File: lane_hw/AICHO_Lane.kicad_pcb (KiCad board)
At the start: 2 copper layers, 0 parts

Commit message: lane_hw: DC-DC
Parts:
- added C11: 10u 50V, Capacitor_SMD:C_0805_2012Metric, F.Cu at (86.3, 50.2)
- added C12: 10u 50V, Capacitor_SMD:C_0805_2012Metric, F.Cu at (84.3, 50.2)
- added C13: 100n, Capacitor_SMD:C_0402_1005Metric, F.Cu at (82.8, 50.8)
- added C14: 100n, Capacitor_SMD:C_0402_1005Metric, F.Cu at (78.5, 49.2)
- added C15: 22u 25V, Capacitor_SMD:C_0805_2012Metric, F.Cu at (77.2, 51.1)
- added C16: 22u 25V, Capacitor_SMD:C_0805_2012Metric, F.Cu at (77.2, 53.1)
- added C17: 33p, Capacitor_SMD:C_0402_1005Metric, F.Cu at (81.3, 47.2)
- added L1: 15u, Inductor_SMD:L_Sunlord_SWPA5040S, F.Cu at (81.8, 55.0)
- added R11: 200k, Resistor_SMD:R_0402_1005Metric, F.Cu at (80.4, 47.2)
- added R12: 27k, Resistor_SMD:R_0402_1005Metric, F.Cu at (79.0, 47.6)
- added U1: TPS54302, Package_TO_SOT_SMD:SOT-23-6, F.Cu at (80.7, 50.2)
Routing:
- net +5V: track 0.00 -> 14.5 mm
- net Net-(U1-SW): track 0.00 -> 10.6 mm, vias 0 -> 2
- net +24V: track 0.00 -> 4.80 mm
- net GND: track 0.00 -> 3.83 mm, vias 0 -> 21
- net Net-(U1-FB): track 0.00 -> 3.32 mm
- net Net-(U1-BOOT): track 0.00 -> 1.37 mm

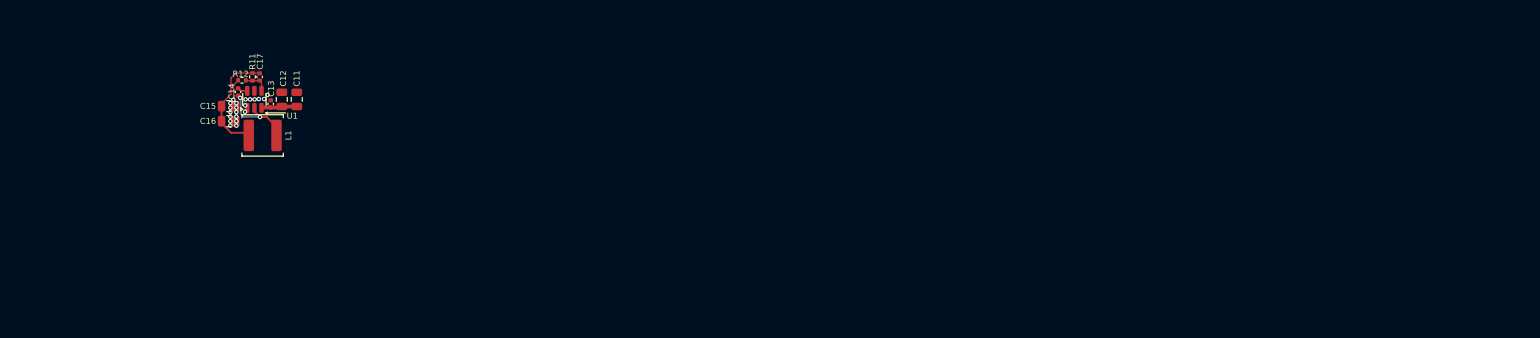
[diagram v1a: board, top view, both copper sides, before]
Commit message: lane_hw: Preliminary layout
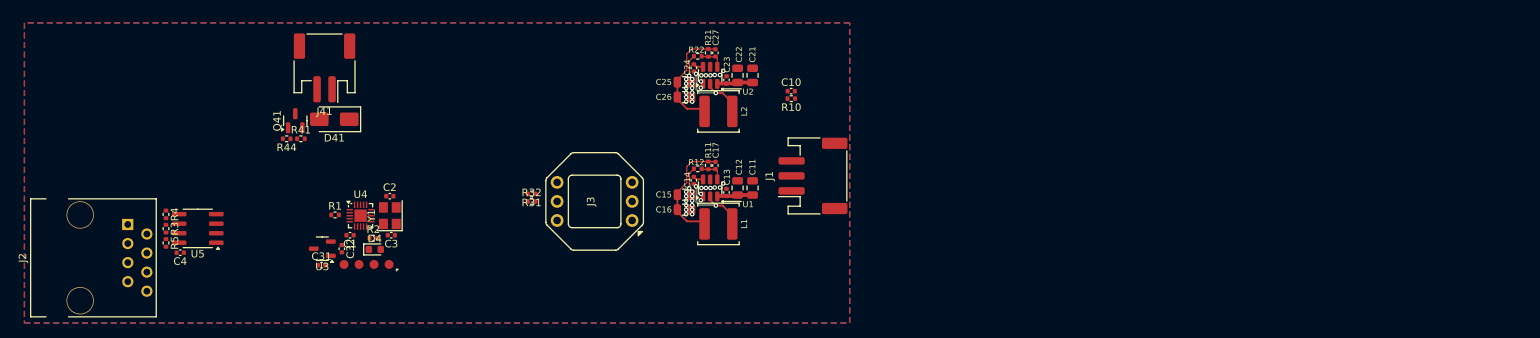
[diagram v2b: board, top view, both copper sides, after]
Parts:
- added C1: 100n, Capacitor_SMD:C_0402_1005Metric, F.Cu at (93.4, 68.3)
- added C10: 100n, Capacitor_SMD:C_0402_1005Metric, F.Cu at (152.2, 49.1)
- added C2: 15p, Capacitor_SMD:C_0402_1005Metric, F.Cu at (98.7, 63.1)
- added C21: 10u 50V, Capacitor_SMD:C_0805_2012Metric, F.Cu at (147.1, 47.0)
- added C22: 10u 50V, Capacitor_SMD:C_0805_2012Metric, F.Cu at (145.1, 47.0)
- added C23: 100n, Capacitor_SMD:C_0402_1005Metric, F.Cu at (143.6, 47.6)
- added C24: 100n, Capacitor_SMD:C_0402_1005Metric, F.Cu at (139.2, 46.0)
- added C25: 22u 25V, Capacitor_SMD:C_0805_2012Metric, F.Cu at (138.0, 47.9)
- added C26: 22u 25V, Capacitor_SMD:C_0805_2012Metric, F.Cu at (138.0, 49.9)
- added C27: 100p, Capacitor_SMD:C_0402_1005Metric, F.Cu at (142.1, 44.0)
- added C3: 15p, Capacitor_SMD:C_0402_1005Metric, F.Cu at (98.9, 68.3)
- added C31: 1u, Capacitor_SMD:C_0402_1005Metric, F.Cu at (89.6, 72.3)
- added C32: 1u, Capacitor_SMD:C_0402_1005Metric, F.Cu at (92.3, 70.1)
- added C4: 100n, Capacitor_SMD:C_0402_1005Metric, F.Cu at (70.8, 70.6)
- added D4: White, LED_SMD:LED_0603_1608Metric, F.Cu at (96.7, 70.2)
- added D41: SS14, Diode_SMD:D_SMA, F.Cu at (91.3, 52.9)
- added J1: JST PH, Connector_JST:JST_PH_S3B-PH-SM4-TB_1x03-1MP_P2.00mm_Horizontal, F.Cu at (155.1, 60.4)
- added J2: RJ45, RJ45:RJ45_OST_PJ012-8P8CX_Vertical, F.Cu at (63.8, 66.9)
- added J3: XGZP6847A, XGZP6847A:XGZP6847A, F.Cu at (126.0, 63.8)
- added J41: JST PH, Connector_JST:JST_PH_S2B-PH-SM4-TB_1x02-1MP_P2.00mm_Horizontal, F.Cu at (90.0, 46.0)
- added J9: Conn_01x04, TestPoints_P2.00:TestPoints_1x04_P2.00, F.Cu at (95.6, 72.2)
- added L2: 15u, Inductor_SMD:L_Sunlord_SWPA5040S, F.Cu at (142.5, 51.8)
- added Q41: AO3400A, Package_TO_SOT_SMD:SOT-23, F.Cu at (86.1, 53.0)
- added R1: 1k, Resistor_SMD:R_0402_1005Metric, F.Cu at (91.4, 65.6)
- added R10: 4.7, Resistor_SMD:R_0402_1005Metric, F.Cu at (152.2, 50.1)
- added R2: 5.1k, Resistor_SMD:R_0402_1005Metric, F.Cu at (96.5, 68.7)
- added R21: 100k, Resistor_SMD:R_0402_1005Metric, F.Cu at (141.2, 44.0)
- added R22: 5.1k, Resistor_SMD:R_0402_1005Metric, F.Cu at (139.8, 44.5)
- added R3: 100, Resistor_SMD:R_0402_1005Metric, F.Cu at (68.9, 67.4)
- added R31: 20k, Resistor_SMD:R_0402_1005Metric, F.Cu at (117.6, 62.8)
- added R32: 51k, Resistor_SMD:R_0402_1005Metric, F.Cu at (117.6, 63.8)
- added R4: 10k, Resistor_SMD:R_0402_1005Metric, F.Cu at (68.9, 65.5)
- added R41: 100k, Resistor_SMD:R_0402_1005Metric, F.Cu at (86.8, 55.5)
- added R44: 100, Resistor_SMD:R_0402_1005Metric, F.Cu at (85.0, 55.5)
- added R5: 10k, Resistor_SMD:R_0402_1005Metric, F.Cu at (68.9, 69.3)
- added U2: TPS54302, Package_TO_SOT_SMD:SOT-23-6, F.Cu at (141.4, 47.0)
- added U3: XC6206P332MR, Package_TO_SOT_SMD:SOT-23-3, F.Cu at (89.7, 70.1)
- added U4: PY32F003F18U6, Package_DFN_QFN:QFN-20-1EP_3x3mm_P0.4mm_EP1.65x1.65mm, F.Cu at (94.8, 65.7)
- added U5: SP485E, Package_SO:SOIC-8_3.9x4.9mm_P1.27mm, F.Cu at (73.1, 67.4)
- added Y1: 16MHz 9pF, Crystal:Crystal_SMD_3225-4Pin_3.2x2.5mm, F.Cu at (98.7, 65.7)
- moved C11 61.9 mm to (147.1, 62.0)
- moved C12 61.9 mm to (145.1, 62.0)
- moved C14 61.9 mm to (139.2, 61.0)
- moved C15 61.9 mm to (138.0, 62.9)
- moved C16 61.9 mm to (138.0, 64.9)
- moved C17 61.9 mm to (142.1, 59.0)
- moved L1 61.9 mm to (142.5, 66.8)
- moved R11 61.9 mm to (141.2, 59.0)
- moved R12 61.9 mm to (139.8, 59.5)
- moved U1 61.9 mm to (141.4, 62.0)
- moved C13 61.9 mm to (143.6, 62.6)
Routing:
- net +12V: track 0.00 -> 14.5 mm
- net Net-(U2-SW): track 0.00 -> 10.6 mm, vias 0 -> 2
- net +24V: track 4.80 -> 9.60 mm
- net GND: track 3.83 -> 7.66 mm, vias 21 -> 42
- net Net-(U2-FB): track 0.00 -> 3.32 mm
- net Net-(U2-BOOT): track 0.00 -> 1.37 mm
- added copper zone on B.Cu, net GND
- added copper zone on F.Cu, net GND

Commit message: lane_hw: Attempting to adjust layout
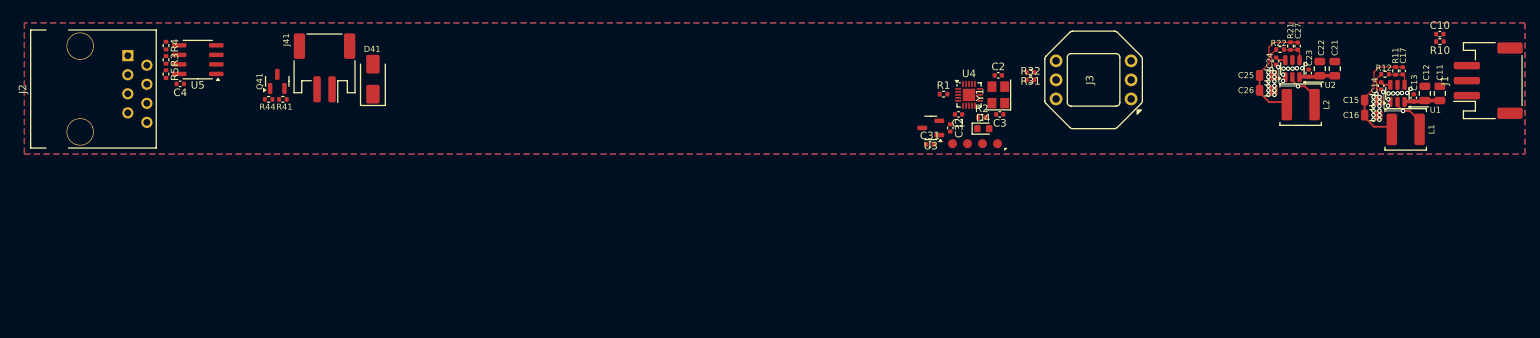
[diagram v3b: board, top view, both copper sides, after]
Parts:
- moved C13 92.5 mm to (235.2, 50.0)
- moved C11 92.5 mm to (238.7, 49.4)
- moved C12 92.5 mm to (236.7, 49.4)
- moved C14 92.5 mm to (230.8, 48.4)
- moved C15 92.5 mm to (229.6, 50.3)
- moved C16 92.5 mm to (229.6, 52.3)
- moved C17 92.5 mm to (233.7, 46.4)
- moved L1 92.5 mm to (234.1, 54.2)
- moved R11 92.5 mm to (232.8, 46.4)
- moved R12 92.5 mm to (231.3, 46.9)
- moved U1 92.5 mm to (233.0, 49.4)
- moved J1 90.9 mm to (245.1, 47.7)
- moved C10 86.8 mm to (238.7, 41.5)
- moved R10 86.8 mm to (238.7, 42.5)
- moved C2 82.7 mm to (179.8, 47.0)
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
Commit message: lane_hw: Reassign pins
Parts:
- moved D4 7.13 mm to (184.9, 53.5), turned to 180 degrees
- moved R1 5.44 mm to (176.9, 52.7), turned to 90 degrees
- moved R2 4.92 mm to (182.4, 53.7)
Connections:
- U4 pad 1: /PUMP_2 -> /UART2_RX
- U4 pad 10: unconnected-(U4-PB6-Pad10) -> /UART1_TX
- U4 pad 16: /UART2_TX -> /PRESSURE_SENSOR
- U4 pad 17: /UART2_RX -> /PUMP_3
- U4 pad 18: /DE -> /PUMP_2
- U4 pad 19: /PRESSURE_SENSOR -> /PUMP_1
- U4 pad 2: /PUMP_3 -> /DE
- U4 pad 20: /PUMP_1 -> /UART2_TX
- U4 pad 3: /UART1_TX -> unconnected-(U4-PA7-Pad3)
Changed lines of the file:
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@@
 	(net 37 "unconnected-(U4-PF2-Pad15)")
 	(net 38 "unconnected-(U4-PB5-Pad9)")
-	(net 39 "unconnected-(U4-PB6-Pad10)")
-	(net 40 "unconnected-(U4-PF4-Pad12)")
+	(net 39 "unconnected-(U4-PF4-Pad12)")
+	(net 40 "unconnected-(U4-PA7-Pad3)")
 	(footprint "Capacitor_SMD:C_0805_2012Metric"
 		(layer "F.Cu")
@@
 	(footprint "Resistor_SMD:R_0402_1005Metric"
 		(layer "F.Cu")
-		(at 172.5 49.5)
+		(at 176.9 52.7 90)
 		(descr "Resistor SMD 0402 (1005 Metric), square (rectangular) end terminal, IPC-7351 nominal, (Body size source: IPC-SM-782 page 72, https://www.pcb-3d.com/wordpress/wp-content/uploads/ipc-sm-782a_amendment_1_and_2.pdf), generated with kicad-footprint-generator")
 		(tags "resistor")
 		(property "Reference" "R1"
-			(at 0 -1.17 0)
+			(at 0 -1.17 90)
 			(layer "F.SilkS")
 			(effects
@@
 		)
 		(property "Value" "1k"
-			(at 0 1.17 0)
+			(at 0 1.17 90)
 			(layer "F.Fab")
 			(effects
@@
 		)
 		(property "Datasheet" ""
-			(at 0 0 0)
+			(at 0 0 90)
 			(layer "F.Fab")
 			(hide yes)
@@
 		)
 		(property "Description" "Resistor"
-			(at 0 0 0)
+			(at 0 0 90)
 			(layer "F.Fab")
 			(hide yes)
@@
 		)
 		(fp_line
-			(start -0.93 -0.47)
-			(end 0.93 -0.47)
+			(start 0.93 -0.47)
+			(end 0.93 0.47)
 			(stroke
 				(width 0.05)
@@
 		)
 		(fp_line
-			(start -0.93 0.47)
-			(end -0.93 -0.47)
+			(start -0.93 -0.47)
+			(end 0.93 -0.47)
 			(stroke
 				(width 0.05)
@@
 		)
 		(fp_line
-			(start 0.93 -0.47)
-			(end 0.93 0.47)
+			(start 0.93 0.47)
+			(end -0.93 0.47)
 			(stroke
 				(width 0.05)
@@
 		)
 		(fp_line
-			(start 0.93 0.47)
-			(end -0.93 0.47)
+			(start -0.93 0.47)
+			(end -0.93 -0.47)
 			(stroke
 				(width 0.05)
@@
 		)
 		(fp_line
-			(start -0.525 -0.27)
-			(end 0.525 -0.27)
+			(start 0.525 -0.27)
+			(end 0.525 0.27)
 			(stroke
 				(width 0.1)
@@
 		)
 		(fp_line
-			(start -0.525 0.27)
-			(end -0.525 -0.27)
+			(start -0.525 -0.27)
+			(end 0.525 -0.27)
 			(stroke
 				(width 0.1)
@@
 		)
 		(fp_line
-			(start 0.525 -0.27)
-			(end 0.525 0.27)
+			(start 0.525 0.27)
+			(end -0.525 0.27)
 			(stroke
 				(width 0.1)
@@
 		)
 		(fp_line
-			(start 0.525 0.27)
-			(end -0.525 0.27)
+			(start -0.525 0.27)
+			(end -0.525 -0.27)
 			(stroke
 				(width 0.1)
@@
 		)
 		(fp_text user "${REFERENCE}"
-			(at 0 0 0)
+			(at 0 0 90)
 			(layer "F.Fab")
 			(effects
@@
 		)
 		(pad "1" smd roundrect
-			(at -0.51 0)
+			(at -0.51 0 90)
 			(size 0.54 0.64)
 			(layers "F.Cu" "F.Mask" "F.Paste")
@@
 		)
 		(pad "2" smd roundrect
-			(at 0.51 0)
+			(at 0.51 0 90)
 			(size 0.54 0.64)
 			(layers "F.Cu" "F.Mask" "F.Paste")
@@
 			(layers "F.Cu" "F.Mask" "F.Paste")
 			(roundrect_rratio 0.25)
-			(net 30 "/PUMP_2")
+			(net 35 "/UART2_RX")
 			(pinfunction "PA5")
 			(pintype "bidirectional")
@@
 			(layers "F.Cu" "F.Mask" "F.Paste")
 			(roundrect_rratio 0.25)
-			(net 31 "/PUMP_3")
+			(net 33 "/DE")
 			(pinfunction "PA6")
 			(pintype "bidirectional")
@@
 			(layers "F.Cu" "F.Mask" "F.Paste")
 			(roundrect_rratio 0.25)
-			(net 26 "/UART1_TX")
+			(net 40 "unconnected-(U4-PA7-Pad3)")
 			(pinfunction "PA7")
-			(pintype "bidirectional")
+			(pintype "bidirectional+no_connect")
 		)
 		(pad "4" smd roundrect
@@
 			(layers "F.Cu" "F.Mask" "F.Paste")
 			(roundrect_rratio 0.25)
-			(net 39 "unconnected-(U4-PB6-Pad10)")
+			(net 26 "/UART1_TX")
 			(pinfunction "PB6")
-			(pintype "bidirectional+no_connect")
+			(pintype "bidirectional")
 		)
 		(pad "11" smd roundrect
@@
 			(layers "F.Cu" "F.Mask" "F.Paste")
 			(roundrect_rratio 0.25)
-			(net 40 "unconnected-(U4-PF4-Pad12)")
+			(net 39 "unconnected-(U4-PF4-Pad12)")
 			(pinfunction "PF4")
 			(pintype "bidirectional+no_connect")
@@
 			(layers "F.Cu" "F.Mask" "F.Paste")
 			(roundrect_rratio 0.25)
-			(net 34 "/UART2_TX")
+			(net 28 "/PRESSURE_SENSOR")
 			(pinfunction "PA0")
 			(pintype "bidirectional")
@@
 			(layers "F.Cu" "F.Mask" "F.Paste")
 			(roundrect_rratio 0.25)
-			(net 35 "/UART2_RX")
+			(net 31 "/PUMP_3")
 			(pinfunction "PA1")
 			(pintype "bidirectional")
@@
 			(layers "F.Cu" "F.Mask" "F.Paste")
 			(roundrect_rratio 0.25)
-			(net 33 "/DE")
+			(net 30 "/PUMP_2")
 			(pinfunction "PA2")
 			(pintype "bidirectional")
@@
 			(layers "F.Cu" "F.Mask" "F.Paste")
 			(roundrect_rratio 0.25)
-			(net 28 "/PRESSURE_SENSOR")
+			(net 29 "/PUMP_1")
 			(pinfunction "PA3")
 			(pintype "bidirectional")
@@
 			(layers "F.Cu" "F.Mask" "F.Paste")
 			(roundrect_rratio 0.25)
-			(net 29 "/PUMP_1")
+			(net 34 "/UART2_TX")
 			(pinfunction "PA4")
 			(pintype "bidirectional")
@@
 	(footprint "LED_SMD:LED_0603_1608Metric"
 		(layer "F.Cu")
-		(at 177.8 54.1)
+		(at 184.9 53.5 180)
 		(descr "LED SMD 0603 (1608 Metric), square (rectangular) end terminal, IPC-7351 nominal, (Body size source: http://www.tortai-tech.com/upload/download/2011102023233369053.pdf), generated with kicad-footprint-generator")
 		(tags "LED")
@@
 		)
 		(property "Sim.Pins" "1=K 2=A"
-			(at 0 0 0)
+			(at 0 0 180)
 			(unlocked yes)
 			(layer "F.Fab")
@@
 		(attr smd)
 		(fp_line
-			(start -1.485 -0.735)
-			(end -1.485 0.735)
+			(start 0.8 -0.735)
+			(end -1.485 -0.735)
 			(stroke
 				(width 0.12)
@@
 		)
 		(fp_line
-			(start 0.8 -0.735)
-			(end -1.485 -0.735)
+			(start -1.485 -0.735)
+			(end -1.485 0.735)
 			(stroke
 				(width 0.12)
@@
 		)
 		(fp_line
-			(start -1.48 -0.73)
-			(end 1.48 -0.73)
+			(start 1.48 0.73)
+			(end -1.48 0.73)
 			(stroke
 				(width 0.05)
@@
 		)
 		(fp_line
-			(start -1.48 0.73)
-			(end -1.48 -0.73)
+			(start 1.48 -0.73)
+			(end 1.48 0.73)
 			(stroke
 				(width 0.05)
@@
 		)
 		(fp_line
-			(start 1.48 -0.73)
-			(end 1.48 0.73)
+			(start -1.48 0.73)
+			(end -1.48 -0.73)
 			(stroke
 				(width 0.05)
@@
 		)
 		(fp_line
-			(start 1.48 0.73)
-			(end -1.48 0.73)
+			(start -1.48 -0.73)
+			(end 1.48 -0.73)
 			(stroke
 				(width 0.05)
@@
 		)
 		(fp_line
-			(start -0.8 -0.1)
-			(end -0.8 0.4)
+			(start 0.8 0.4)
+			(end 0.8 -0.4)
 			(stroke
 				(width 0.1)
@@
 		)
 		(fp_line
-			(start -0.8 0.4)
-			(end 0.8 0.4)
+			(start 0.8 -0.4)
+			(end -0.5 -0.4)
 			(stroke
 				(width 0.1)
@@
 		)
 		(fp_line
-			(start 0.8 -0.4)
-			(end -0.5 -0.4)
+			(start -0.8 0.4)
+			(end 0.8 0.4)
 			(stroke
 				(width 0.1)
@@
 		)
 		(fp_line
-			(start 0.8 0.4)
-			(end 0.8 -0.4)
+			(start -0.8 -0.1)
+			(end -0.8 0.4)
 			(stroke
 				(width 0.1)
@@
 		)
 		(pad "1" smd roundrect
-			(at -0.7875 0)
+			(at -0.7875 0 180)
 			(size 0.875 0.95)
 			(layers "F.Cu" "F.Mask" "F.Paste")
@@
 		)
 		(pad "2" smd roundrect
-			(at 0.7875 0)
+			(at 0.7875 0 180)
 			(size 0.875 0.95)
 			(layers "F.Cu" "F.Mask" "F.Paste")
@@
 	(footprint "Resistor_SMD:R_0402_1005Metric"
 		(layer "F.Cu")
-		(at 177.6 52.6)
+		(at 182.4 53.7)
 		(descr "Resistor SMD 0402 (1005 Metric), square (rectangular) end terminal, IPC-7351 nominal, (Body size source: IPC-SM-782 page 72, https://www.pcb-3d.com/wordpress/wp-content/uploads/ipc-sm-782a_amendment_1_and_2.pdf), generated with kicad-footprint-generator")
 		(tags "resistor")

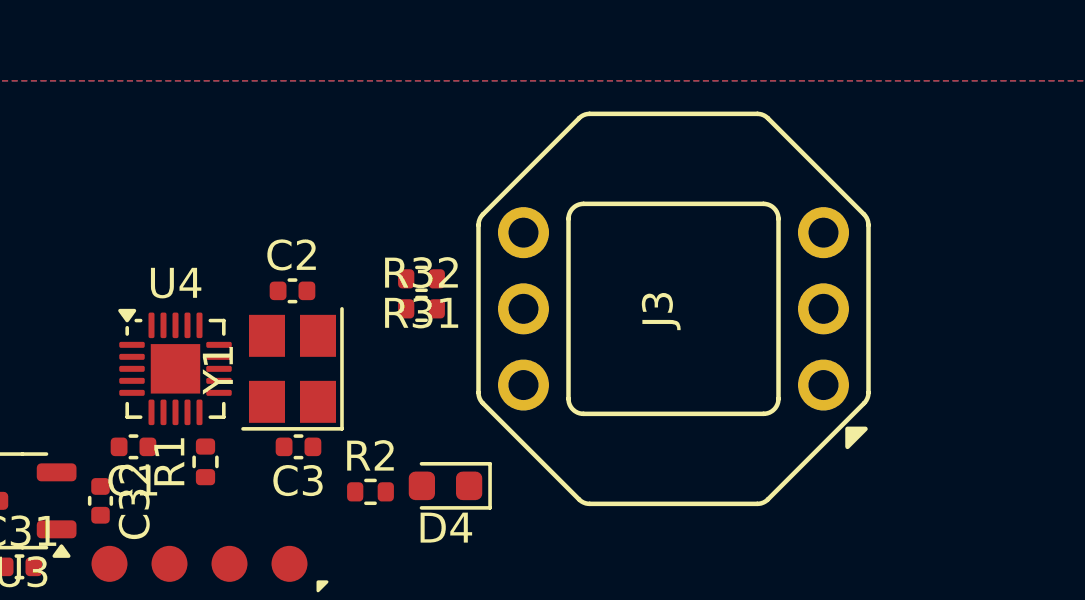
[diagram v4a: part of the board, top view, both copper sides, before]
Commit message: lane_hw: Add capacitors around pressure sensor
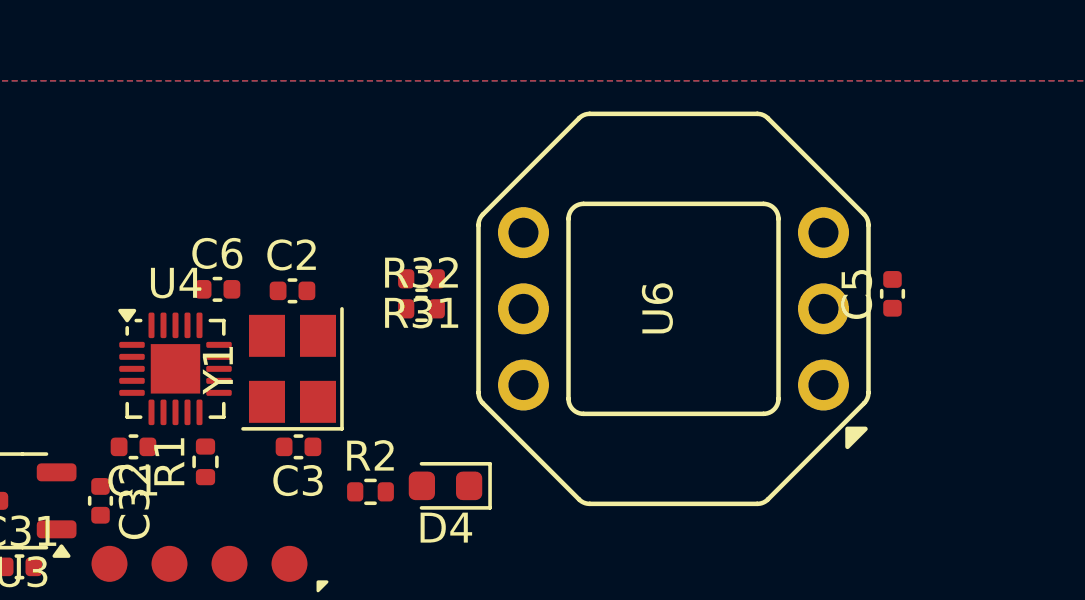
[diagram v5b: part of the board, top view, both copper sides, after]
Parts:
- added C5: 1u, Capacitor_SMD:C_0402_1005Metric, F.Cu at (199.8, 47.1)
- added C6: 10n, Capacitor_SMD:C_0402_1005Metric, F.Cu at (177.3, 47.0)
- renumbered J3 to U6

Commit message: lane_hw: Further layout
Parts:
- added C28: 220u 25V, Capacitor_SMD:CP_Elec_6.3x7.7, F.Cu at (142.8, 46.9)
- added C5: 100n, Capacitor_SMD:C_0402_1005Metric, F.Cu at (71.2, 48.1)
- added D42: SS14, Diode_SMD:D_SMA, F.Cu at (136.4, 47.5)
- added D43: SS14, Diode_SMD:D_SMA, F.Cu at (176.4, 47.5)
- added J42: JST PH, Connector_JST:JST_PH_S2B-PH-SM4-TB_1x02-1MP_P2.00mm_Horizontal, F.Cu at (130.0, 46.0)
- added J43: JST PH, Connector_JST:JST_PH_S2B-PH-SM4-TB_1x02-1MP_P2.00mm_Horizontal, F.Cu at (170.0, 46.0)
- added Q42: AO3400A, Package_TO_SOT_SMD:SOT-23, F.Cu at (123.7, 47.8)
- added Q43: AO3400A, Package_TO_SOT_SMD:SOT-23, F.Cu at (163.7, 47.8)
- added R42: 100k, Resistor_SMD:R_0402_1005Metric, F.Cu at (124.5, 50.2)
- added R43: 100k, Resistor_SMD:R_0402_1005Metric, F.Cu at (164.4, 50.2)
- added R45: 100, Resistor_SMD:R_0402_1005Metric, F.Cu at (122.5, 50.2)
- added R46: 100, Resistor_SMD:R_0402_1005Metric, F.Cu at (162.6, 50.2)
- C4: value 100n -> 1u
- moved L2 70.4 mm to (149.8, 46.6), turned to 90 degrees
- moved C21 70.2 mm to (154.6, 51.2), turned to 0 degrees
- moved C22 68.1 mm to (154.6, 49.2), turned to 0 degrees
- moved C23 67.2 mm to (154.0, 47.7), turned to 0 degrees
- moved U2 64.4 mm to (154.6, 45.5), turned to 0 degrees
- moved C26 64.2 mm to (151.7, 42.1), turned to -90 degrees
- moved C27 62.2 mm to (157.6, 46.2), turned to 180 degrees
- moved C25 62.1 mm to (153.7, 42.1), turned to -90 degrees
- moved C24 61.2 mm to (155.6, 43.4), turned to 180 degrees
- moved R21 61.2 mm to (157.6, 45.3), turned to 180 degrees
- moved R22 60.2 mm to (157.2, 43.9), turned to 90 degrees
- moved C31 25.2 mm to (191.5, 41.9), turned to 180 degrees
- moved U3 22.9 mm to (191.4, 44.1), turned to 0 degrees
- moved C32 18.3 mm to (188.8, 44.1), turned to 90 degrees
- moved J9 15.5 mm to (183.8, 42.2), turned to 0 degrees
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- renumbered C5 to C6, C6 to C7
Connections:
- U4 pad 11: /ACT_LED -> unconnected-(U4-PB7-Pad11)
- U4 pad 16: /PRESSURE_SENSOR -> /ACT_LED
- U4 pad 3: unconnected-(U4-PA7-Pad3) -> /PRESSURE_SENSOR
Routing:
- net /DE: track 0.00 -> 127.0 mm
- net /UART2_TX: track 0.00 -> 122.0 mm
- net /UART2_RX: track 0.00 -> 119.9 mm
- net /PUMP_1: track 0.00 -> 107.4 mm
- net +5V: track 14.5 -> 100.2 mm
- net +12V: track 14.5 -> 95.8 mm
- net /PUMP_2: track 0.00 -> 66.7 mm
- net /PUMP_3: track 0.00 -> 26.0 mm
- net Net-(D43-A): track 0.00 -> 15.2 mm
- net Net-(D41-A): track 0.00 -> 15.2 mm
- net Net-(D42-A): track 0.00 -> 15.2 mm
- net +24V: track 9.60 -> 21.3 mm
- net /RS485_A: track 0.00 -> 7.79 mm
- net /PRESSURE_SENSOR: track 0.00 -> 7.09 mm
- net +3V3: track 0.00 -> 6.16 mm
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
